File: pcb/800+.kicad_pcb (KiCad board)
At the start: 2 copper layers, 50.5 x 195.6 mm, 113 parts, among them J1 2inch LCD, J2 USB_B_Micro, J3 MSP_SBW, J4 Cradle, J5 Battery, J6 Conn_01x18, Q1 S8050, Q2 AO3401A, SW1 Off, SW10 R_LCD3, SW11 R_LCD4, SW12 LCD_LEFT, SW13 LCD_RIGHT, SW14 Glow, SW15 Device, SW16 Media, SW17 Mute, SW18 Prev, SW19 Vol+, SW2 Activities, SW20 Vol-, SW21 Ch+, SW22 Ch-, SW23 Dpad_Up, SW24 Dpad_Left, SW25 Dpad_Right, SW26 Dpad_Down, SW27 Dpad_OK, SW28 PgUp, SW29 PgDown, SW3 Help, SW30 Menu, SW31 Exit, SW32 Guide, SW33 Info, SW34 Stop, SW35 Replay, SW36 Skip, SW37 Play, SW38 Rec, SW39 Rew, SW4 L_LCD1, SW40 Fwd, SW41 Pause, SW42 KP_1, SW43 KP_2, SW44 KP_3, SW45 KP_4, SW46 KP_5, SW47 KP_6, SW48 KP_7, SW49 KP_8, SW5 L_LCD2, SW50 KP_9, SW51 KP_0, SW52 KP_Clear, SW53 KP_Enter, SW6 L_LCD3, SW7 L_LCD4, SW8 R_LCD1, SW9 R_LCD2, U1 MSP430G2553IPW28

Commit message: alpha2 pcb
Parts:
- added C5: 10u, Capacitor_SMD:C_0805_2012Metric, B.Cu at (97.5, 64.8)
- added C6: 10u, Capacitor_SMD:C_0805_2012Metric, B.Cu at (86.1, 70.5)
- added C7: 1u, Capacitor_SMD:C_0805_2012Metric, B.Cu at (120.4, 81.1)
- added F1: Polyfuse, Resistor_SMD:R_1210_3225Metric_Pad1.30x2.65mm_HandSolder, B.Cu at (99.9, 59.7)
- added J7: ESP_PROG, Connector_PinHeader_2.54mm:PinHeader_1x06_P2.54mm_Vertical, F.Cu at (100.7, 104.8)
- added R7: 1M, Resistor_SMD:R_0805_2012Metric, B.Cu at (93.8, 47.3)
- added R8: 10k, Resistor_SMD:R_0805_2012Metric, B.Cu at (95.9, 102.6)
- added R9: 10k, Resistor_SMD:R_0805_2012Metric, B.Cu at (120.8, 88.8)
- added TP1: TestPoint, TestPoint:TestPoint_THTPad_D2.5mm_Drill1.2mm, F.Cu at (97.7, 55.0)
- added U2: ESP32-S3-WROOM-1U, PCM_Espressif:ESP32-S3-WROOM-1, B.Cu at (109.1, 88.4)
- added U3: USBLC6, Package_TO_SOT_SMD:SOT-23-6, B.Cu at (104.8, 56.3)
- added U4: AP1117, Package_TO_SOT_SMD:SOT-223, B.Cu at (90.9, 70.4)
- D1, D10, D11, D12, D13, D14, D15, D16, D17, D18, D19, D2, D20, D21, D22, D23, D24, D25, D26, D27, D28, D29, D3, D30, D31, D32, D4, D5, D6, D7, D8, D9: footprint 880+:C265_reverse_mount_led -> 880+:C265_reverse_mount_led_DRC
- J6: value Conn_01x18 -> ESP_JTAG; footprint 880+:ESP_TestPad -> Connector_PinHeader_2.54mm:PinHeader_1x06_P2.54mm_Vertical; moved to F.Cu
- moved J6 38.6 mm to (100.7, 102.1), turned to 90 degrees
- moved R3 27.3 mm to (91.4, 91.6), turned to 0 degrees
- moved Q1 27.0 mm to (92.8, 88.3), turned to 180 degrees
- moved R1 26.9 mm to (95.6, 91.3), turned to 0 degrees
- moved R2 16.6 mm to (96.4, 85.3), turned to 180 degrees
- moved Q2 6.48 mm to (93.9, 95.3)
- moved R6 5.79 mm to (89.6, 97.8)
- moved C1 5.54 mm to (97.5, 67.3), turned to 180 degrees
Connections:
- C1 pad 2: +3V3 -> +3.3V
- C3 pad 1: +3V3 -> +3.3V
- C4 pad 1: +3V3 -> +3.3V
- J1 pad 3: +3V3 -> +3.3V
- J1 pad 4: +3V3 -> +3.3V
- J2 pad 1: unconnected-(J2-Pad1) -> Net-(J2-VBUS)
- J2 pad 2: unconnected-(J2-Pad2) -> /DN
- J2 pad 3: unconnected-(J2-Pad3) -> /DP
- J2 pad 5: unconnected-(J2-Pad5) -> GND
- J2 pad 6: unconnected-(J2-Pad6) -> Net-(J2-Shield)
- J3 pad 2: +3V3 -> +3.3V
- J6 pad 1: +3V3 -> +3.3V
- J6 pad 3: /LCD_BLC -> TCK
- J6 pad 4: /LCD_D/C -> TDO
- J6 pad 5: /LCD_CS -> TDI
- J6 pad 6: /LCD_CLK -> TMS
- Q2 pad 2: /LED_TP -> +3.3V
- Q2 pad 3: +3V3 -> /LED_TP
- R3 pad 1: +3V3 -> +3.3V
- R4 pad 1: +3V3 -> +3.3V
- R5 pad 2: +3V3 -> +3.3V
- U1 pad 1: +3V3 -> +3.3V
- U1 pad 2: MSP_P1.0 -> ESP_EN
- U1 pad 3: MSP_P1.1 -> ESP_TO_MSP
- U1 pad 4: MSP_P1.2 -> MSP_TO_ESP
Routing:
- net GND: track 781.3 -> 1096.6 mm, vias 111 -> 145
- net +3.3V: track 0.00 -> 219.6 mm, vias 0 -> 9
- net +3V3: track 153.2 -> 0.00 mm, vias 8 -> 0
- net ESP_EN: track 0.00 -> 77.6 mm, vias 0 -> 1
- net MSP_P1.2: track 67.8 -> 0.00 mm
- net MSP_TO_ESP: track 0.00 -> 66.1 mm
- net ESP_TO_MSP: track 0.00 -> 65.8 mm, vias 0 -> 2
- net MSP_P1.1: track 64.6 -> 0.00 mm
- net MSP_P1.0: track 55.8 -> 0.00 mm
- net D-: track 0.00 -> 48.0 mm
- net D+: track 0.00 -> 47.8 mm
- net ESP_RXD: track 0.00 -> 30.0 mm, vias 0 -> 2
- net ESP_TXD: track 0.00 -> 29.7 mm, vias 0 -> 1
- net TMS: track 0.00 -> 26.5 mm, vias 0 -> 1
- net /LCD_BLC: track 30.9 -> 5.96 mm
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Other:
- board text added: "3V3-3V3 GND-GND TCK-BOOT TDO-RxD TDI-TxD TMS-EN"
- board text added: "800+ Alpha2"
- board text added: "880+ Alpha2"
- board text added: "GND 3V3 GND DIO TCK"
- board text added: "JTAG PGRM"
- board text removed: "3v3 GND LCD_BL LCD_D/C LCD CS LCD CLK LCD DIN LCD_RST P1.7 P1.6 P1.5 P1.4 P1.3 P1.2 P1.1 P1.0 LED_TP LED_DRIVE"

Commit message: current working kikad
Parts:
- added REF**: SOIC-8_7.5x5.85mm_P1.27mm, Package_SO:SOIC-8_7.5x5.85mm_P1.27mm, F.Cu at (39.4, 46.7)
- added REF**: SOP-8_3.9x4.9mm_P1.27mm, Package_SO:SOP-8_3.9x4.9mm_P1.27mm, F.Cu at (39.5, 57.9)

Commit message: parts placed
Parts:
- removed H2, H3: Programming JTAG, MountingHole:MountingHole_3mm
- removed REF**: SOIC-8_7.5x5.85mm_P1.27mm, Package_SO:SOIC-8_7.5x5.85mm_P1.27mm
- removed REF**: SOP-8_3.9x4.9mm_P1.27mm, Package_SO:SOP-8_3.9x4.9mm_P1.27mm
- removed TP1: TestPoint, TestPoint:TestPoint_THTPad_D2.5mm_Drill1.2mm
- added BZ1: 5020 Passive, 880+:5020passiveBuzzer, B.Cu at (116.6, 60.2)
- added C10: 1.0uF, Capacitor_SMD:C_0805_2012Metric, B.Cu at (99.5, 105.6)
- added C11: 0.1uF, Capacitor_SMD:C_0805_2012Metric, B.Cu at (106.7, 152.4)
- added C12: 4.7uF, Capacitor_SMD:C_0805_2012Metric, B.Cu at (97.8, 150.1)
- added C13: 4.7uF, Capacitor_SMD:C_0805_2012Metric, B.Cu at (106.7, 157.2)
- added C14: 2.2uF, Capacitor_SMD:C_0805_2012Metric, B.Cu at (92.5, 105.8)
- added C15: 0.1uF, Capacitor_SMD:C_0805_2012Metric, B.Cu at (83.2, 105.8)
- added C16: 1.0uF, Capacitor_SMD:C_0805_2012Metric, B.Cu at (85.3, 105.8)
- added C17: 1u, Capacitor_SMD:C_0805_2012Metric, B.Cu at (105.3, 226.3)
- added C8: 2.2uF, Capacitor_SMD:C_0805_2012Metric, B.Cu at (105.9, 103.5)
- added C9: 0.1uF, Capacitor_SMD:C_0805_2012Metric, B.Cu at (102.8, 102.7)
- added D10: LED, 880+:C265_reverse_mount_led_DRC, B.Cu at (104.8, 144.2)
- added D11: LED, 880+:C265_reverse_mount_led_DRC, B.Cu at (98.3, 136.1)
- added D20: LED, 880+:C265_reverse_mount_led_DRC, B.Cu at (98.6, 144.5)
- added D21: LED, 880+:C265_reverse_mount_led_DRC, B.Cu at (101.5, 154.8)
- added D22: LED, 880+:C265_reverse_mount_led_DRC, B.Cu at (111.2, 153.2)
- added D31: LED, 880+:C265_reverse_mount_led_DRC, B.Cu at (83.1, 148.7)
- added D33: LED, 880+:C265_reverse_mount_led_DRC, B.Cu at (86.1, 134.3)
- added D36: LED, 880+:C265_reverse_mount_led_DRC, B.Cu at (119.5, 148.2)
- added D37: LED, 880+:C265_reverse_mount_led_DRC, B.Cu at (91.6, 153.0)
- added D43: LED, 880+:C265_reverse_mount_led_DRC, B.Cu at (97.3, 185.7)
- added D44: LED, 880+:C265_reverse_mount_led_DRC, F.Cu at (324.3, 62.5)
- added D9: LED, 880+:C265_reverse_mount_led_DRC, B.Cu at (104.8, 136.0)
- added F2: Polyfuse, Resistor_SMD:R_1210_3225Metric_Pad1.30x2.65mm_HandSolder, B.Cu at (88.1, 55.0)
- added IR1: LED, 880+:IR_led, B.Cu at (93.4, 46.5)
- added IR2: LED, 880+:IR_led, B.Cu at (109.8, 46.0)
- added Q3: AO3401A, Package_TO_SOT_SMD:SOT-23, B.Cu at (113.7, 54.3)
- added Q4: AO3401A, Package_TO_SOT_SMD:SOT-23, B.Cu at (119.9, 66.5)
- added R10: 10k, Resistor_SMD:R_0805_2012Metric, B.Cu at (116.8, 54.6)
- added R11: R, Resistor_SMD:R_0805_2012Metric, B.Cu at (80.4, 73.2)
- added R12: R, Resistor_SMD:R_0805_2012Metric, B.Cu at (82.5, 73.2)
- added R13: 2k, Resistor_SMD:R_0805_2012Metric, B.Cu at (98.1, 147.0)
- added R14: 22, Resistor_SMD:R_1210_3225Metric, B.Cu at (91.7, 50.4)
- added R15: 22, Resistor_SMD:R_1210_3225Metric, B.Cu at (112.6, 49.3)
- added R16: 4.7k, Resistor_SMD:R_0805_2012Metric, B.Cu at (115.1, 139.1)
- added R17: 4.7k, Resistor_SMD:R_0805_2012Metric, B.Cu at (115.1, 141.1)
- added R18: 10k, Resistor_SMD:R_0805_2012Metric, B.Cu at (122.9, 66.4)
- added R19: 4.7k, Resistor_SMD:R_0805_2012Metric, B.Cu at (112.5, 70.4)
- added R20: 4.7k, Resistor_SMD:R_0805_2012Metric, B.Cu at (112.5, 68.5)
- added R21: 0, Resistor_SMD:R_1206_3216Metric, B.Cu at (111.9, 59.3)
- added SW54: Red, 880+:4mm Dome, F.Cu at (322.2, 38.1)
- added SW55: Blue, 880+:4mm Dome, F.Cu at (322.2, 44.2)
- added SW56: SW_RollingBall, Resistor_SMD:R_1210_3225Metric, B.Cu at (94.7, 122.3)
- added TVS1: P6SMB12CA, Diode_SMD:D_SMB, B.Cu at (83.1, 62.2)
- added U10: MAX17048, 880+:TDFN-8-1EP_2x2mm_P0.5mm_EP0.8x1.4mm, B.Cu at (108.3, 149.6)
- added U11: MCP73831, Package_TO_SOT_SMD:SOT-23-5, B.Cu at (101.9, 149.1)
- added U12: VEML7700-TR, 880+:VEML7700, B.Cu at (104.9, 58.0)
- added U5: LM66200DRLR, Package_TO_SOT_SMD:SOT-583-8, B.Cu at (96.9, 63.4)
- added U6: LM66200DRLR, Package_TO_SOT_SMD:SOT-583-8, B.Cu at (104.0, 63.2)
- added U7: TSOP75340TT, 880+:IR_input, B.Cu at (101.5, 228.5)
- added U8: SPX3819M5-L, Package_TO_SOT_SMD:SOT-23-5, B.Cu at (81.5, 68.7)
- added U9: RT9080-3.3, Package_TO_SOT_SMD:SOT-23-5, B.Cu at (102.8, 105.5)
- C5: value 10u -> .1u
- J4: value Cradle -> Battery; footprint Connector_JST:JST_GH_BM03B-GHS-TBT_1x03-1MP_P1.25mm_Vertical -> 880+:Battery_reuse
- J5: value Battery -> Cradle; footprint 880+:Battery_reuse -> Connector_JST:JST_GH_BM03B-GHS-TBT_1x03-1MP_P1.25mm_Vertical
- J6, J7: moved to B.Cu
- Q1: value S8050 -> AO3401A
- R1: value 10R -> 10k
- R2: value 1k -> 10; footprint Resistor_SMD:R_0805_2012Metric -> Resistor_SMD:R_1210_3225Metric
- R3: value 10k -> R
- R6: value R -> 10
- SW28: value PgUp -> PgUp/Grn
- SW29: value PgDown -> PgDown/Yel
- U3: value USBLC6 -> USBLC6-2
- U4: value AP1117 -> RT9080-3.3; footprint Package_TO_SOT_SMD:SOT-223 -> Package_TO_SOT_SMD:SOT-23-5
- moved J4 99.3 mm to (97.4, 158.7)
- moved J5 98.1 mm to (89.6, 60.9)
- moved J6 79.0 mm to (100.2, 181.1), turned to 180 degrees
- moved J7 76.3 mm to (102.9, 181.1), turned to 180 degrees
- moved R6 69.2 mm to (117.5, 161.1), turned to -90 degrees
- moved Q2 65.9 mm to (117.7, 156.7)
- moved R3 62.7 mm to (97.4, 153.9), turned to -90 degrees
- moved R5 61.9 mm to (120.9, 156.6), turned to -90 degrees
- moved D32 54.9 mm to (116.8, 134.2)
- moved U4 35.5 mm to (89.0, 105.8), turned to 180 degrees
- moved C6 30.5 mm to (115.6, 78.5), turned to 180 degrees
- moved C5 24.0 mm to (115.6, 80.5), turned to 180 degrees
- moved C3 23.7 mm to (111.5, 118.6), turned to 180 degrees
- moved C4 21.5 mm to (111.5, 120.6), turned to 180 degrees
- moved U1 20.5 mm to (109.6, 126.8)
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- renumbered D9 to D12, D10 to D13, D11 to D14, D12 to D15, D13 to D16, D14 to D17, D15 to D18, D16 to D19, D17 to D23, D18 to D24, D19 to D25, D20 to D26, D21 to D27, D22 to D28, D23 to D29, D24 to D30, D25 to D34, D26 to D35, D27 to D38, D28 to D39, D29 to D40, D30 to D41, D31 to D42
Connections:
- net /DN renamed /Power/DN
- net /DP renamed /Power/DP
- net /LED_TP renamed Net-(Q2-D)
- net Net-(J2-Shield) renamed /Power/Shield
- net Net-(J2-VBUS) renamed /Power/Vbus
- C1 pad 2: +3.3V -> +3.3VP
- C5 pad 1: +5V -> +3.3VP
- C6 pad 1: +3.3V -> +3.3VP
- C7 pad 1: GND -> ESP_EN
- C7 pad 2: ESP_EN -> GND
- F1 pad 1: +5V -> /Power/USB_input
- J1 pad 2: /LCD_BL -> GND
- J1 pad 3: +3.3V -> /LEDA
- J1 pad 4: +3.3V -> +3.3VP
- J4 pad 1: unconnected-(J4-Pin_1-Pad1) -> VBATT
- J4 pad 2: unconnected-(J4-Pin_2-Pad2) -> BatteryTemp
- J4 pad 3: unconnected-(J4-Pin_3-Pad3) -> GND
- J5 pad 1: unconnected-(J5-Pin_1-Pad1) -> Net-(J5-Pin_1)
- J5 pad 2: unconnected-(J5-Pin_2-Pad2) -> GND
- J6 pad 1: +3.3V -> +3.3VP
- J7 pad 1: +3.3V -> +3.3VP
- Q1 pad 1: Net-(Q1-B) -> /LCD_BLC
- Q1 pad 2: GND -> +3.3VP
- Q1 pad 3: Net-(Q1-C) -> Net-(Q1-D)
- Q2 pad 2: +3.3V -> +3.3VP
- R1 pad 1: Net-(Q1-C) -> /LCD_BLC
- R1 pad 2: /LCD_BL -> +3.3VP
- R2 pad 1: /LCD_BLC -> Net-(Q1-D)
- R2 pad 2: Net-(Q1-B) -> /LEDA
- R3 pad 2: Net-(Q1-B) -> BatteryTemp
- R5 pad 2: +3.3V -> +3.3VP
- R8 pad 2: +3.3V -> +3.3VP
- R9 pad 2: +3.3V -> +3.3VP
- U1 pad 2: ESP_EN -> BatteryTemp
- U1 pad 22: MSP_P1.6 -> FuelGauge_SCL
- U1 pad 23: MSP_P1.7 -> FuelGauge_SDA
- U1 pad 26: unconnected-(U1-XOUT/P2.7-Pad26) -> Net-(U1-XOUT/P2.7)
- U1 pad 3: ESP_TO_MSP -> FuelGauge_Alert
- U1 pad 5: MSP_P1.3 -> BatteryPowered
- U1 pad 6: MSP_P1.4 -> ChargeStatus
- U1 pad 7: MSP_P1.5 -> 3v3VP_Enable
- U2 pad 10: ESP_TO_MSP -> unconnected-(U2-GPIO17/U1TXD/ADC2_CH6-Pad10)
- U2 pad 12: MSP_P1.7 -> GND
- U2 pad 2: +3.3V -> +3.3VP
- U2 pad 23: GND -> IR_input
- U2 pad 24: GND -> 5V_Supply
- U2 pad 38: GND -> IR_output
- U2 pad 4: MSP_P1.5 -> Buzzer_output
- U2 pad 5: MSP_P1.4 -> GND
- U2 pad 6: MSP_P1.3 -> GND
- U2 pad 7: MSP_P1.6 -> GND
- U2 pad 8: GND -> LightSensor_SDA
- U2 pad 9: GND -> LightSensor_SCL
- U4 pad 1: GND -> VIN
- U4 pad 2: +3.3V -> GND
- U4 pad 3: +5V -> 3v3VP_Enable
- U4 pad 4: +3.3V -> unconnected-(U4-NC-Pad4)
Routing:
- net GND: track 1096.6 -> 0.24 mm, vias 145 -> 0
- net LED_PWM: track 506.1 -> 0.00 mm, vias 27 -> 0
- net B: track 268.2 -> 0.00 mm, vias 15 -> 0
- net 2: track 261.5 -> 0.00 mm, vias 7 -> 0
- net A: track 239.9 -> 0.00 mm, vias 17 -> 0
- net D: track 229.8 -> 0.00 mm, vias 17 -> 0
- net 1: track 229.1 -> 0.00 mm, vias 4 -> 0
- net +3.3V: track 219.6 -> 0.00 mm, vias 9 -> 0
- net 3: track 207.8 -> 0.00 mm, vias 4 -> 0
- net C: track 197.4 -> 0.00 mm, vias 15 -> 0
- net 5: track 147.3 -> 0.00 mm, vias 6 -> 0
- net G: track 132.5 -> 0.00 mm, vias 11 -> 0
- net E: track 124.2 -> 0.00 mm, vias 9 -> 0
- net H: track 124.0 -> 0.00 mm, vias 11 -> 0
- net 6: track 122.4 -> 0.00 mm, vias 9 -> 0
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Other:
- board text added: "locked"
- board text removed: "3V3-3V3 GND-GND TCK-BOOT TDO-RxD TDI-TxD TMS-EN"
- board text removed: "800+ Alpha2"
- board text removed: "880+ Alpha2"
- board text removed: "GND 3V3 GND DIO TCK"
- board text removed: "JTAG PGRM"

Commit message: alpha3 pcb
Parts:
- added C18: 1u, Capacitor_SMD:C_0805_2012Metric, B.Cu at (101.7, 60.2)
- moved D44 147.2 mm to (177.7, 76.7)
- moved SW54 147.1 mm to (177.5, 64.6)
- moved SW55 147.1 mm to (177.5, 70.8)
- moved U3 6.36 mm to (104.8, 54.4)
- moved C13 1.70 mm to (108.3, 157.1)
- moved C1 1.35 mm to (98.5, 66.8)
- moved R7 1.21 mm to (108.5, 47.8)
- moved R4 0.36 mm to (92.3, 130.8)
- moved U2 0.35 mm to (103.5, 89.6)
- moved C2 0.32 mm to (92.3, 134.2)
- moved R19 0.12 mm to (112.5, 70.5)
- moved C7 0.10 mm to (114.7, 85.5)
- moved R9 0.10 mm to (116.6, 83.6)
- turned D33 to -80 degrees
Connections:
- U1 pad 3: FuelGauge_Alert -> ChargeStatus
- U1 pad 6: ChargeStatus -> FuelGauge_Alert
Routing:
- net GND: track 0.24 -> 1252.5 mm, vias 0 -> 175
- net LED_PWM: track 0.00 -> 690.7 mm, vias 0 -> 22
- net +3.3VP: track 0.00 -> 303.6 mm, vias 0 -> 15
- net 2: track 0.00 -> 293.1 mm, vias 0 -> 13
- net 1: track 0.00 -> 268.0 mm, vias 0 -> 13
- net B: track 0.00 -> 262.3 mm, vias 0 -> 23
- net D: track 0.00 -> 262.1 mm, vias 0 -> 27
- net C: track 0.00 -> 242.1 mm, vias 0 -> 19
- net A: track 0.00 -> 234.7 mm, vias 0 -> 17
- net 3: track 0.00 -> 232.4 mm, vias 0 -> 7
- net 5: track 0.00 -> 202.2 mm, vias 0 -> 21
- net E: track 0.00 -> 188.4 mm, vias 0 -> 17
- net ESP_EN: track 0.00 -> 162.1 mm, vias 0 -> 3
- net 6: track 0.00 -> 161.0 mm, vias 0 -> 13
- net G: track 0.00 -> 157.7 mm, vias 0 -> 15
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
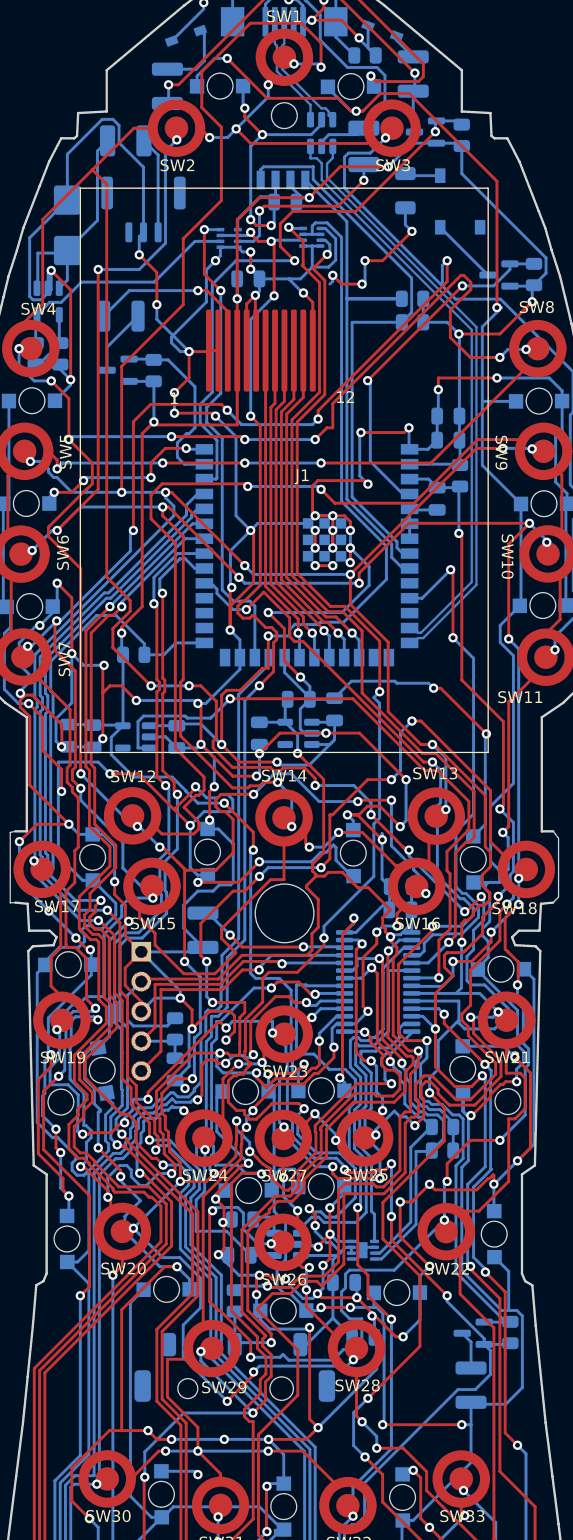
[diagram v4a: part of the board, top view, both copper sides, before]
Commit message: fix VEML7700 direction
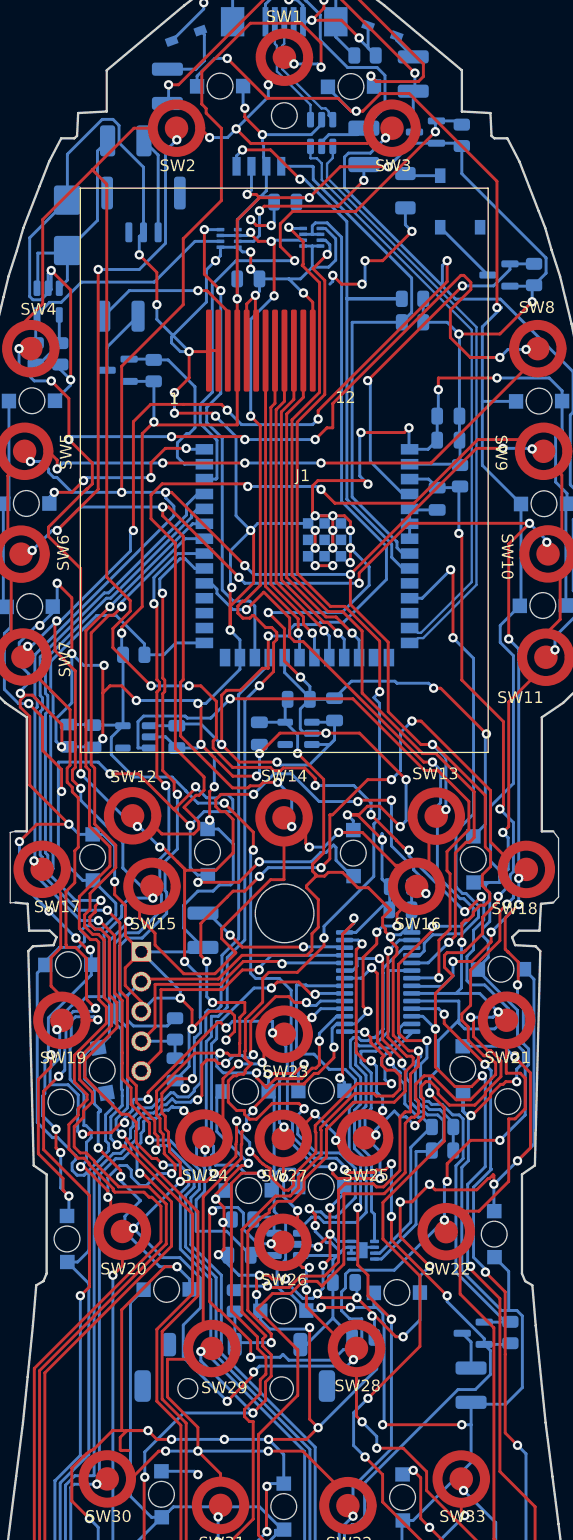
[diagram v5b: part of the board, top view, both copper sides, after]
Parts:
- moved U12 8.86 mm to (96.0, 57.6), turned to 0 degrees
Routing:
- net LightSensor_SCL: track 46.5 -> 54.5 mm, vias 0 -> 2
- net LightSensor_SDA: track 48.9 -> 46.2 mm
- net +3.3VP: track 303.6 -> 305.4 mm, vias 15 -> 16
- net GND: track 1252.5 -> 1253.5 mm
